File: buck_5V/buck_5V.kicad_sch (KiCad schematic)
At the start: 11 parts, among them U901 MT2499A

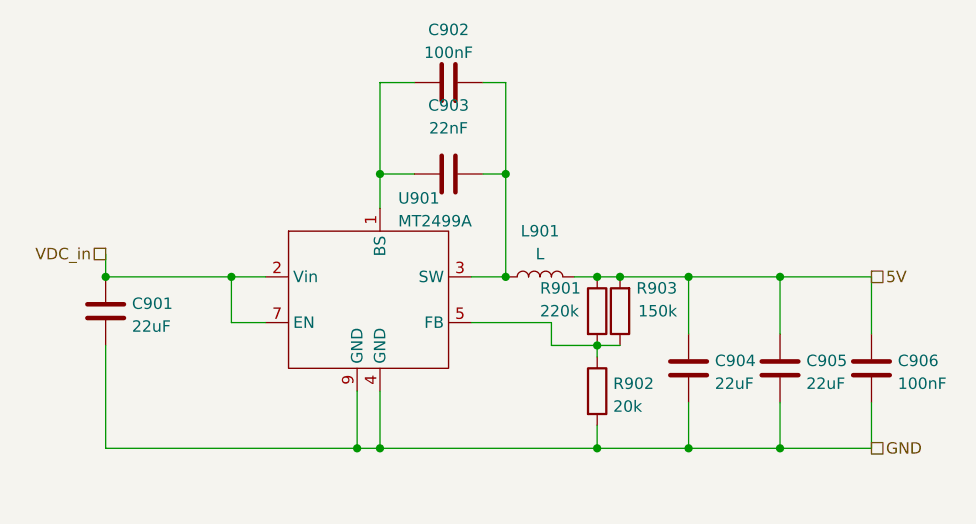
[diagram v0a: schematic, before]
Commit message: added 12V boost converter (300mA max!)
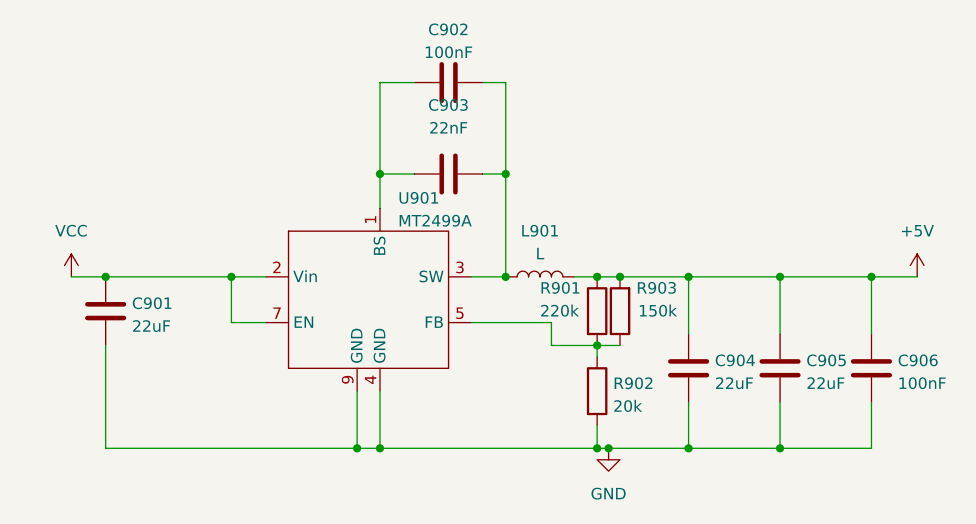
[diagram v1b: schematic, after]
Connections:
- net 5V renamed +5V
- net VDC_in renamed VCC
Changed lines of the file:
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@@
 (kicad_sch (version 20230121) (generator eeschema)
   (paper "A4")
+  (junction (at 176.53 93.98) (diameter 0) (color 0 0 0 0)
+  )
+  (junction (at 176.53 74.93) (diameter 0) (color 0 0 0 0)
+  )
+  (junction (at 166.37 74.93) (diameter 0) (color 0 0 0 0)
+  )
+  (junction (at 115.57 74.93) (diameter 0) (color 0 0 0 0)
+  )
+  (junction (at 186.69 74.93) (diameter 0) (color 0 0 0 0)
+  )
+  (junction (at 158.75 74.93) (diameter 0) (color 0 0 0 0)
+  )
+  (junction (at 157.48 93.98) (diameter 0) (color 0 0 0 0)
+  )
   (junction (at 101.6 74.93) (diameter 0) (color 0 0 0 0)
   )
-  (junction (at 176.53 93.98) (diameter 0) (color 0 0 0 0)
-  )
-  (junction (at 176.53 74.93) (diameter 0) (color 0 0 0 0)
-  )
-  (junction (at 166.37 74.93) (diameter 0) (color 0 0 0 0)
-  )
-  (junction (at 115.57 74.93) (diameter 0) (color 0 0 0 0)
-  )
-  (junction (at 158.75 74.93) (diameter 0) (color 0 0 0 0)
-  )
   (junction (at 156.21 82.55) (diameter 0) (color 0 0 0 0)
   )
@@
     (stroke (width 0) (type default))
   )
-  (wire (pts (xy 166.37 93.98) (xy 156.21 93.98))
+  (wire (pts (xy 166.37 93.98) (xy 157.48 93.98))
     (stroke (width 0) (type default))
   )
@@
     (stroke (width 0) (type default))
   )
+  (wire (pts (xy 191.77 74.93) (xy 186.69 74.93))
+    (stroke (width 0) (type default))
+  )
   (wire (pts (xy 129.54 93.98) (xy 101.6 93.98))
     (stroke (width 0) (type default))
@@
     (stroke (width 0) (type default))
   )
+  (wire (pts (xy 176.53 88.9) (xy 176.53 93.98))
+    (stroke (width 0) (type default))
+  )
   (wire (pts (xy 101.6 74.93) (xy 115.57 74.93))
     (stroke (width 0) (type default))
   )
-  (wire (pts (xy 176.53 88.9) (xy 176.53 93.98))
-    (stroke (width 0) (type default))
-  )
   (wire (pts (xy 166.37 74.93) (xy 176.53 74.93))
     (stroke (width 0) (type default))
@@
     (stroke (width 0) (type default))
   )
-  (wire (pts (xy 101.6 72.39) (xy 101.6 74.93))
+  (wire (pts (xy 97.79 74.93) (xy 101.6 74.93))
     (stroke (width 0) (type default))
   )
@@
     (stroke (width 0) (type default))
   )
+  (wire (pts (xy 157.48 93.98) (xy 156.21 93.98))
+    (stroke (width 0) (type default))
+  )
   (wire (pts (xy 151.13 82.55) (xy 156.21 82.55))
     (stroke (width 0) (type default))
@@
   (wire (pts (xy 142.24 80.01) (xy 151.13 80.01))
     (stroke (width 0) (type default))
-  )
-  (hierarchical_label "5V" (shape passive) (at 186.69 74.93 0) (fields_autoplaced)
-    (effects (font (size 1.27 1.27)) (justify left))
-  )
-  (hierarchical_label "GND" (shape passive) (at 186.69 93.98 0) (fields_autoplaced)
-    (effects (font (size 1.27 1.27)) (justify left))
-  )
-  (hierarchical_label "VDC_in" (shape passive) (at 101.6 72.39 180) (fields_autoplaced)
-    (effects (font (size 1.27 1.27)) (justify right))
   )
   (symbol (lib_id "Device:C") (at 139.7 63.5 90) (unit 1)
@@
     )
   )
+  (symbol (lib_id "power:VCC") (at 97.79 74.93 0) (unit 1)
+    (in_bom yes) (on_board yes) (dnp no) (fields_autoplaced)
+    (property "Reference" "#PWR0103" (at 97.79 78.74 0)
+      (effects (font (size 1.27 1.27)) hide)
+    )
+    (property "Value" "VCC" (at 97.79 69.85 0)
+      (effects (font (size 1.27 1.27)))
+    )
+    (property "Footprint" "" (at 97.79 74.93 0)
+      (effects (font (size 1.27 1.27)) hide)
+    )
+    (property "Datasheet" "" (at 97.79 74.93 0)
+      (effects (font (size 1.27 1.27)) hide)
+    )
+    (pin "1")
+    (instances
+      (project "buck_5V"
+        (path "/d1cb43a0-bc81-49bf-86a7-735d10d531df"
+          (reference "#PWR0103") (unit 1)
+        )
+      )
+    )
+  )
   (symbol (lib_id "Device:C") (at 176.53 85.09 0) (unit 1)
     (in_bom yes) (on_board yes) (dnp no) (fields_autoplaced)
@@
         (path "/e777d9ec-d073-4229-a9e6-2cf85636e407/891f98c0-3628-49fd-a4d5-1cf0156a22a0"
           (reference "C1505") (unit 1)
+        )
+      )
+    )
+  )
+  (symbol (lib_id "power:+5V") (at 191.77 74.93 0) (unit 1)
+    (in_bom yes) (on_board yes) (dnp no) (fields_autoplaced)
+    (property "Reference" "#PWR0102" (at 191.77 78.74 0)
+      (effects (font (size 1.27 1.27)) hide)
+    )
+    (property "Value" "+5V" (at 191.77 69.85 0)
+      (effects (font (size 1.27 1.27)))
+    )
+    (property "Footprint" "" (at 191.77 74.93 0)
+      (effects (font (size 1.27 1.27)) hide)
+    )
+    (property "Datasheet" "" (at 191.77 74.93 0)
+      (effects (font (size 1.27 1.27)) hide)
+    )
+    (pin "1")
+    (instances
+      (project "buck_5V"
+        (path "/d1cb43a0-bc81-49bf-86a7-735d10d531df"
+          (reference "#PWR0102") (unit 1)
         )
       )
@@
         )
       )
+    )
+  )
+  (symbol (lib_id "power:GND") (at 157.48 93.98 0) (unit 1)
+    (in_bom yes) (on_board yes) (dnp no) (fields_autoplaced)
+    (property "Reference" "#PWR0101" (at 157.48 100.33 0)
+      (effects (font (size 1.27 1.27)) hide)
+    )
+    (property "Value" "GND" (at 157.48 99.06 0)
+      (effects (font (size 1.27 1.27)))
+    )
+    (property "Footprint" "" (at 157.48 93.98 0)
+      (effects (font (size 1.27 1.27)) hide)
+    )
+    (property "Datasheet" "" (at 157.48 93.98 0)
+      (effects (font (size 1.27 1.27)) hide)
+    )
+    (pin "1")
+    (instances
+      (project "buck_5V"
+        (path "/d1cb43a0-bc81-49bf-86a7-735d10d531df"
+          (reference "#PWR0101") (unit 1)
+        )
+      )
